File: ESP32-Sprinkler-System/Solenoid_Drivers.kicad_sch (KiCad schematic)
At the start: 40 parts, among them J201 Solenoid, J202 Solenoid, J203 Solenoid, J204 Solenoid, Q201 NCE6005AR, Q202 NCE6005AR, Q203 NCE6005AR, Q204 NCE6005AR, U201 MCP1416T-E/OT, U202 MCP1416T-E/OT, U203 MCP1416T-E/OT, U204 MCP1416T-E/OT

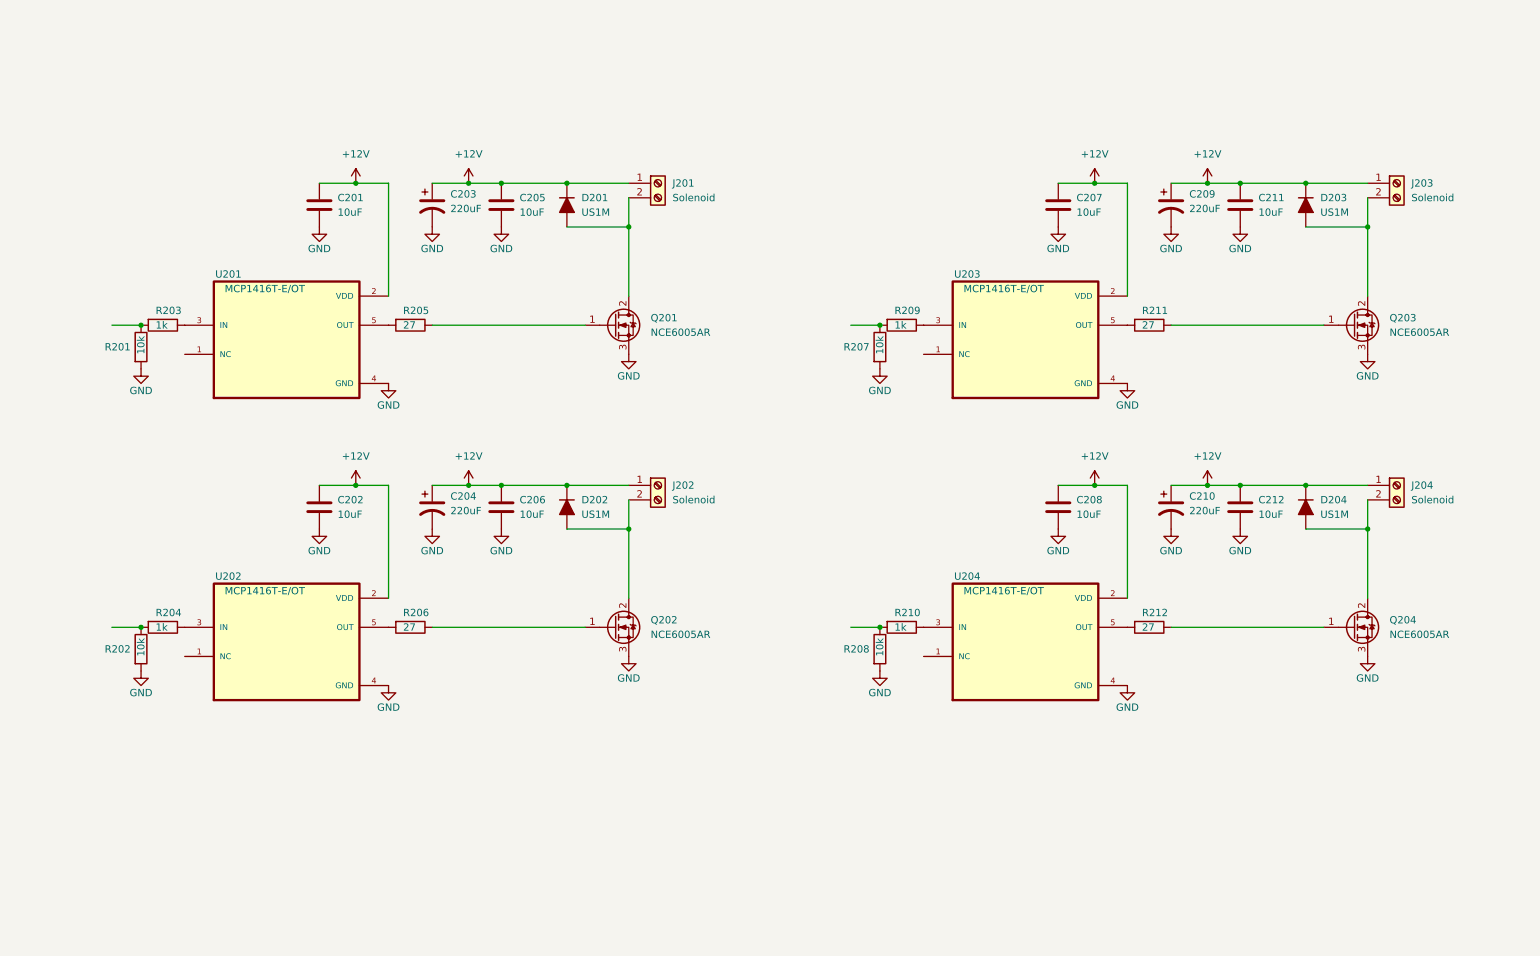
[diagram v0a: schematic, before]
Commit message: Continued working on schematic
finished solenoid drivers, finished buck converter, started ESP32
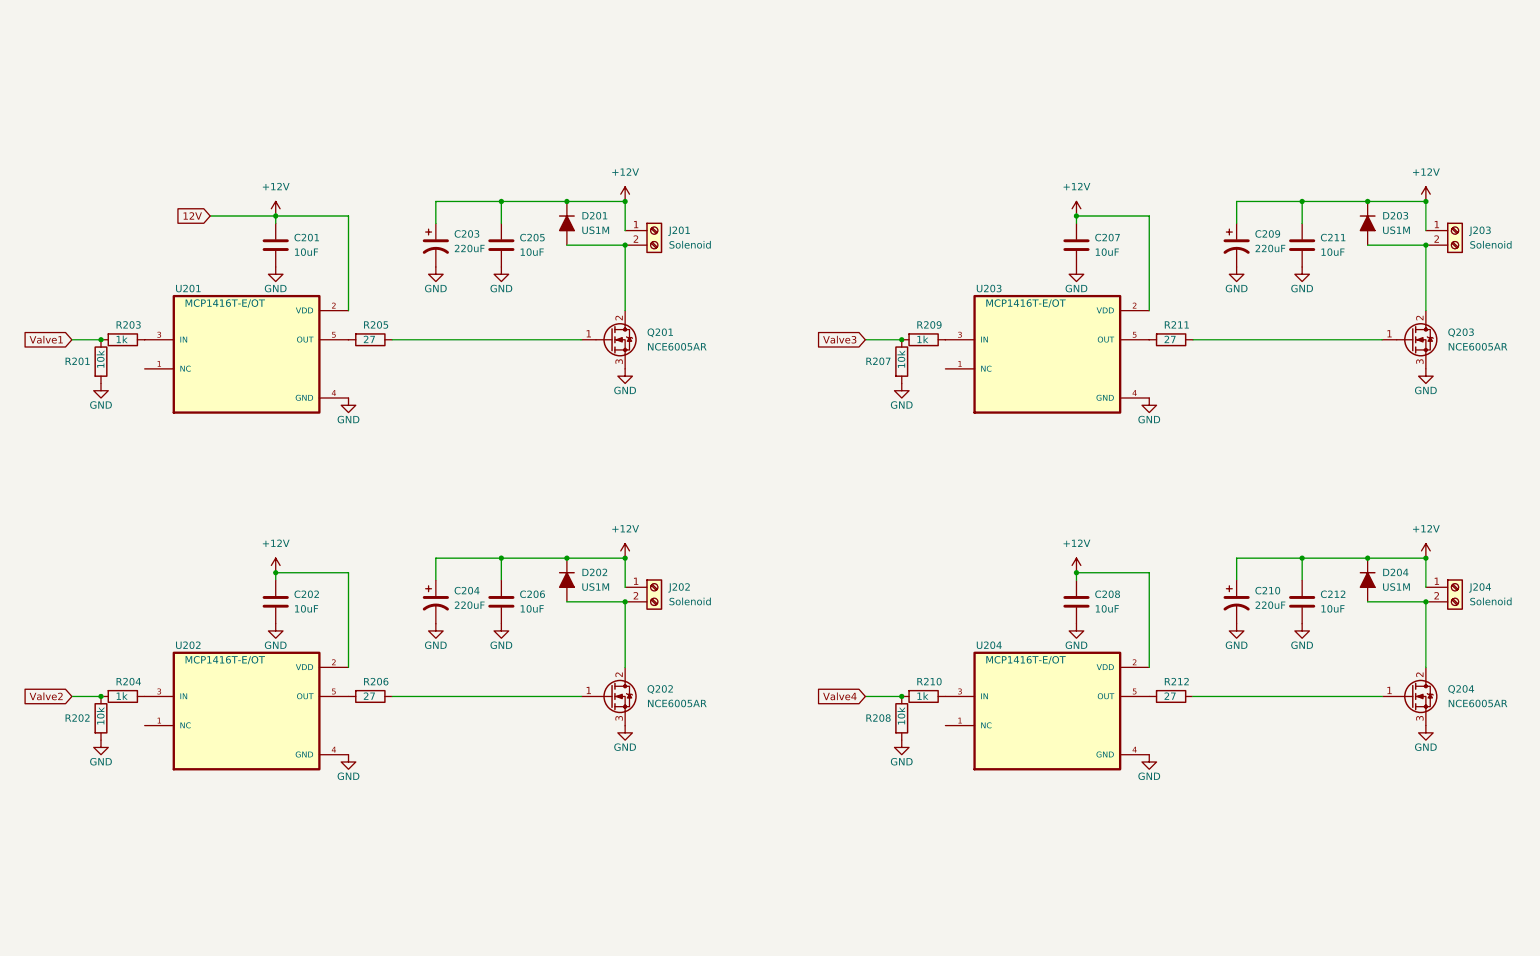
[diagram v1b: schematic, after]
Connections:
- net Valve3: now reaches R207.1, R209.2
- net Valve1: now reaches R201.1, R203.2
- net Valve4: now reaches R208.1, R210.2
- net Valve2: now reaches R202.1, R204.2
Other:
- moved on the sheet: C201, C203, C205, D201, J201, Q201, R201, R203, R205, U201

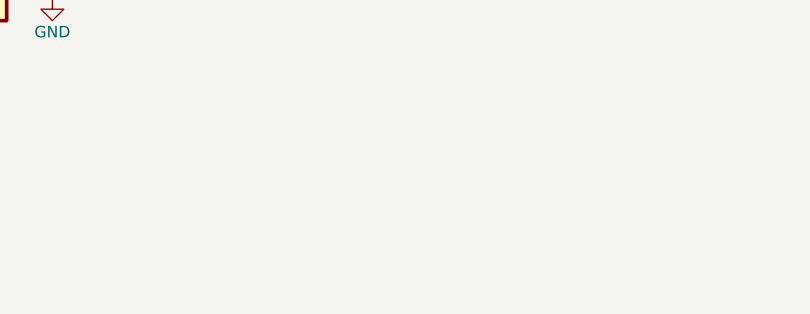
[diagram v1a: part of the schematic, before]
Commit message: Change of plans
We had a change of plans. Rather than having everything made of surface-mount parts, we opted for a simpler through-hole project that could be breadboarded first. This circuit will be revisited and updated when the prototype is complete.
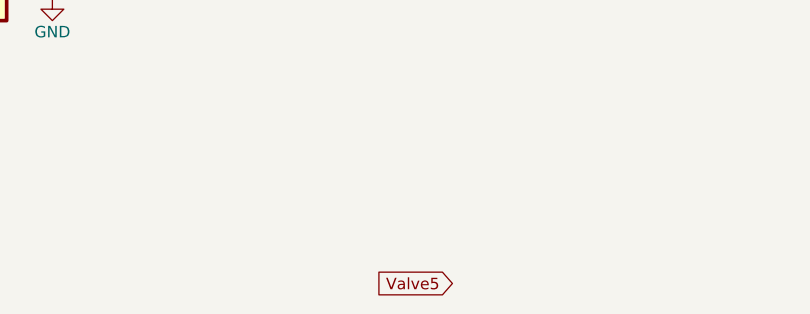
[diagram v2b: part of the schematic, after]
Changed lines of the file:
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@@
+    )
+  )
+  (global_label "Valve5" (shape input) (at 120.65 177.8 180) (fields_autoplaced)
+    (effects (font (size 1.27 1.27)) (justify right))
+    (property "Intersheet References" "${INTERSHEET_REFS}" (id 0) (at 112.0683 177.7206 0)
+      (effects (font (size 1.27 1.27)) (justify right) hide)
     )
   )

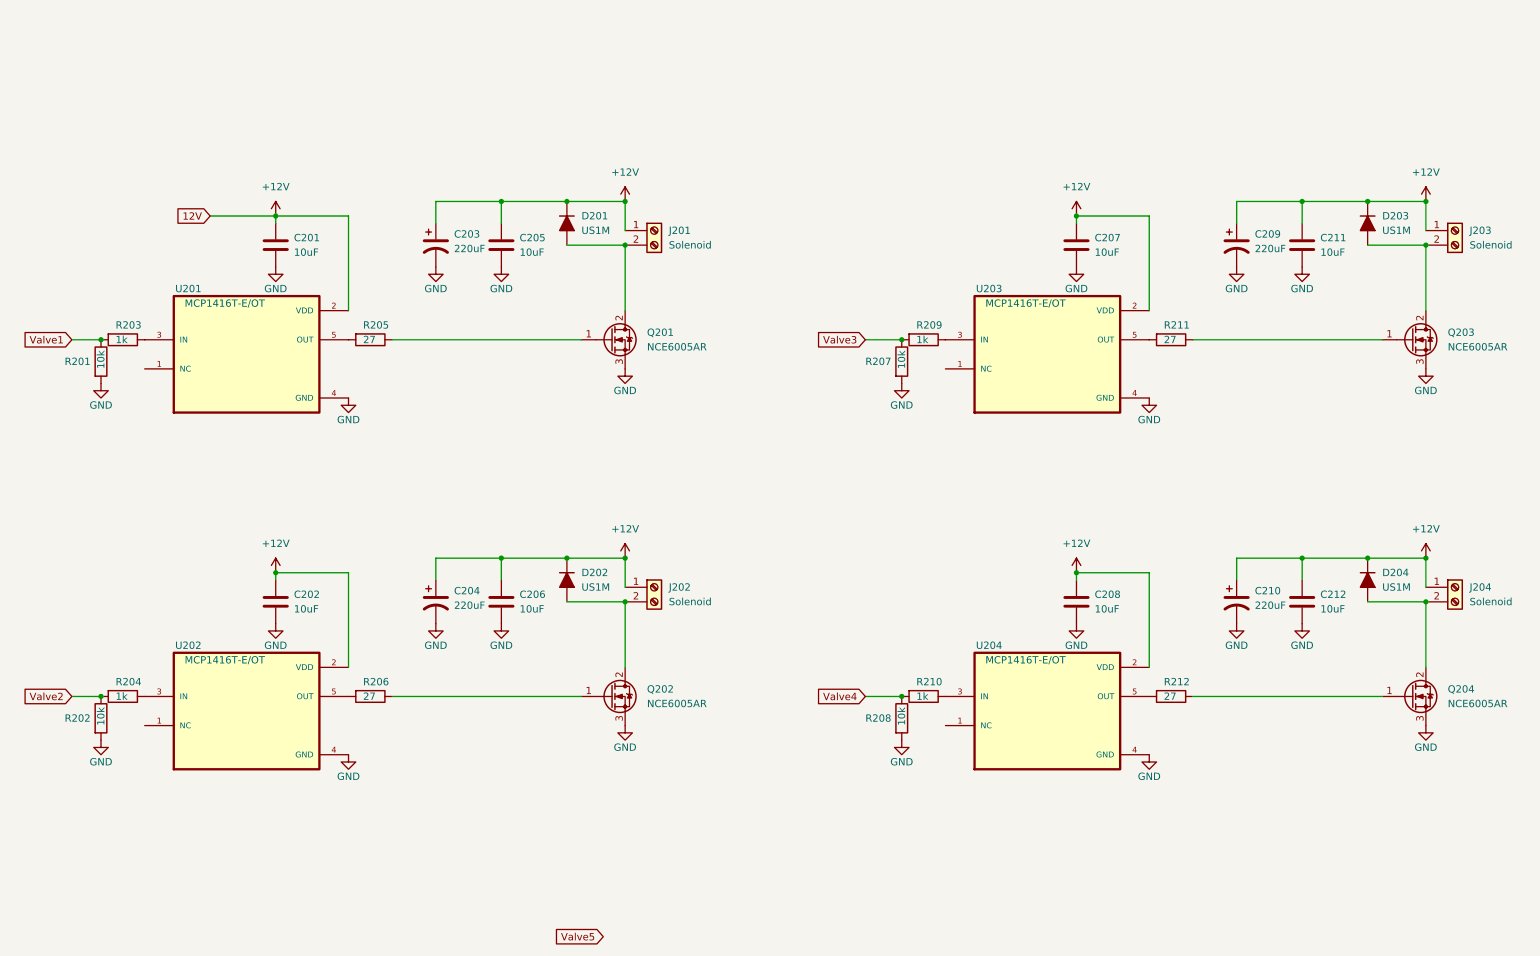
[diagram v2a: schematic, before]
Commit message: Major Update to New Through-Hole Components
Circuit has been modified to match the breadboard prototype Cody built.
Solenoid driver side is done.
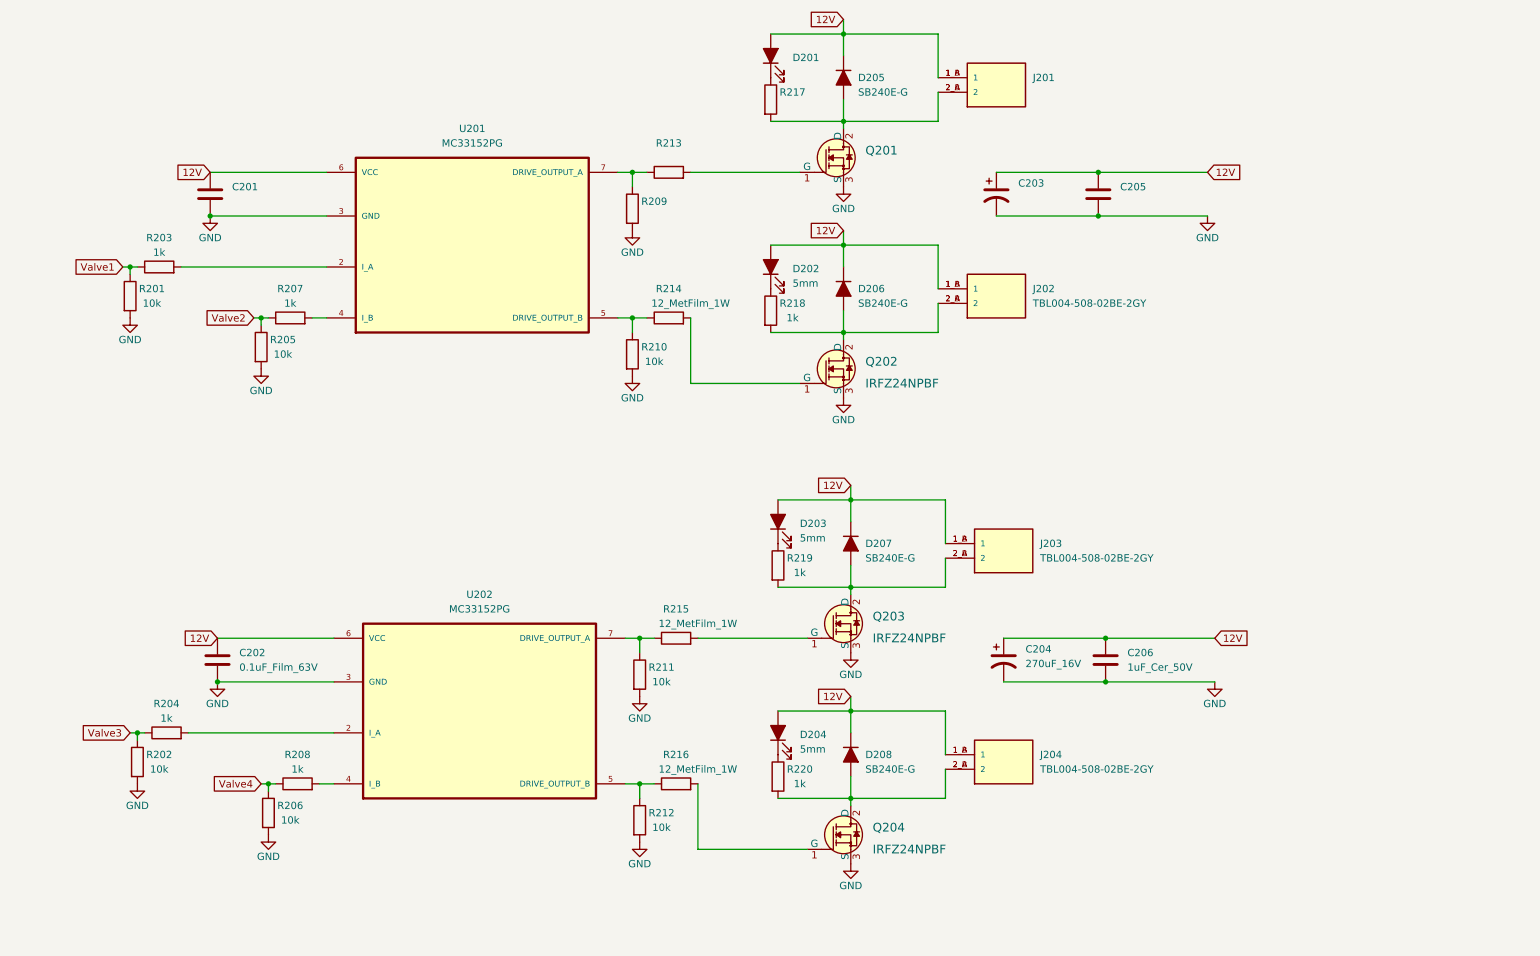
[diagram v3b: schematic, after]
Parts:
- removed C207, C208, C211, C212: 10uF, Capacitor_SMD:C_0603_1608Metric, symbol Device:C
- removed C209, C210: 220uF, Capacitor_SMD:CP_Elec_10x10, symbol Device:C_Polarized_US
- removed D201, D202, D203, D204: US1M, Diode_SMD:D_SMA, symbol Device:D_Filled
- removed J201, J202, J203, J204: Solenoid, Breadstick Footprints:KF202-50-2P, symbol Connector:Screw_Terminal_01x02
- removed Q201, Q202, Q203, Q204: NCE6005AR, Package_TO_SOT_SMD:SOT-223-3_TabPin2, symbol Transistor_FET:BSP89
- removed U201, U202, U203, U204: MCP1416T-E/OT, MCP1416T-E_OT:SOT95P270X145-5N, symbol MCP1416T-E_OT:MCP1416T-E/OT
- added D201: (no value), symbol Device:LED_Filled
- added D202, D203, D204: 5mm, LED_THT:LED_D5.0mm, symbol Device:LED_Filled
- added D205, D206, D207, D208: SB240E-G, Diode_THT:D_DO-15_P12.70mm_Horizontal, symbol Device:D_Filled
- added J201: (no value), symbol TBL004-508-02BE-2GY:TBL004-508-02BE-2GY
- added J202, J203, J204: TBL004-508-02BE-2GY, TBL004-508-02BE-2GY:CUI_TBL004-508-02BE-2GY, symbol TBL004-508-02BE-2GY:TBL004-508-02BE-2GY
- added Q201: (no value), symbol dk_Transistors-FETs-MOSFETs-Single:IRF510PBF
- added Q202, Q203, Q204: IRFZ24NPBF, Package_TO_SOT_THT:TO-220-3_Vertical, symbol dk_Transistors-FETs-MOSFETs-Single:IRF510PBF
- added R213: (no value), symbol Device:R
- added R214, R215, R216: 12_MetFilm_1W, Resistor_THT:R_Axial_DIN0207_L6.3mm_D2.5mm_P10.16mm_Horizontal, symbol Device:R
- added R217: (no value), Resistor_THT:R_Axial_DIN0207_L6.3mm_D2.5mm_P10.16mm_Horizontal, symbol Device:R
- added R218, R219, R220: 1k, Resistor_THT:R_Axial_DIN0207_L6.3mm_D2.5mm_P10.16mm_Horizontal, symbol Device:R
- added U201, U202: MC33152PG, Package_DIP:DIP-8_W7.62mm, symbol MC33152PG:MC33152PG
- C201, C205: value 10uF -> (none); footprint Capacitor_SMD:C_0603_1608Metric -> (none); JLCPCB P/N C96446 -> (none)
- C202: value 10uF -> 0.1uF_Film_63V; footprint Capacitor_SMD:C_0603_1608Metric -> Capacitor_THT:C_Rect_L7.0mm_W2.5mm_P5.00mm; JLCPCB P/N C96446 -> (none)
- C203: value 220uF -> (none); footprint Capacitor_SMD:CP_Elec_10x10 -> (none); JLCPCB P/N C125977 -> (none)
- C204: value 220uF -> 270uF_16V; footprint Capacitor_SMD:CP_Elec_10x10 -> Capacitor_THT:CP_Radial_D6.3mm_P2.50mm; JLCPCB P/N C125977 -> (none)
- C206: value 10uF -> 1uF_Cer_50V; footprint Capacitor_SMD:C_0603_1608Metric -> Capacitor_THT:C_Disc_D7.5mm_W4.4mm_P5.00mm; JLCPCB P/N C96446 -> (none)
- R201, R202: footprint Breadstick Footprints:Perfect_0402_Resistor -> Resistor_THT:R_Axial_DIN0207_L6.3mm_D2.5mm_P10.16mm_Horizontal; JLCPCB P/N C25744 -> (none)
- R203, R204: footprint Breadstick Footprints:Perfect_0402_Resistor -> Resistor_THT:R_Axial_DIN0207_L6.3mm_D2.5mm_P10.16mm_Horizontal; JLCPCB P/N C11702 -> (none)
- R205, R206, R211, R212: value 27 -> 10k; footprint Breadstick Footprints:Perfect_0402_Resistor -> Resistor_THT:R_Axial_DIN0207_L6.3mm_D2.5mm_P10.16mm_Horizontal; JLCPCB P/N C25100 -> (none)
- R207, R208: value 10k -> 1k; footprint Breadstick Footprints:Perfect_0402_Resistor -> Resistor_THT:R_Axial_DIN0207_L6.3mm_D2.5mm_P10.16mm_Horizontal; JLCPCB P/N C25744 -> (none)
- R209: value 1k -> (none); footprint Breadstick Footprints:Perfect_0402_Resistor -> Resistor_THT:R_Axial_DIN0207_L6.3mm_D2.5mm_P10.16mm_Horizontal; JLCPCB P/N C11702 -> (none)
- R210: value 1k -> 10k; footprint Breadstick Footprints:Perfect_0402_Resistor -> Resistor_THT:R_Axial_DIN0207_L6.3mm_D2.5mm_P10.16mm_Horizontal; JLCPCB P/N C11702 -> (none)
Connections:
- net GND: now also R205.2, R206.2, R209.2, R210.2, R211.2, R212.2, Q201.3 (S), Q202.3 (S), Q203.3 (S), Q204.3 (S), U201.3 (GND), U202.3 (GND); no longer R207.2, R208.2
- net Valve1: now also R203.1; no longer R203.2
- net Valve2: now also R205.1, R207.1; no longer R202.1, R204.2
- net Valve3: now also R202.1, R204.1; no longer R207.1, R209.2
- net Valve4: now also R206.1; no longer R210.2
- net at R212.1: now also R216.1, U202.5 (DRIVE_OUTPUT_B)
- net at R209.1: now also R213.1, U201.7 (DRIVE_OUTPUT_A)
- net at R211.1: now also R215.1, U202.7 (DRIVE_OUTPUT_A)
- net at R210.1: now also R214.1, U201.5 (DRIVE_OUTPUT_B)
- net +12V renamed 12V
- net 12V: now also D201.2 (A), D202.2 (A), D203.2 (A), D204.2 (A), D205.1 (K), D206.1 (K), D207.1 (K), D208.1 (K), J201.1_A (1), J201.1_B (1), J202.1_A (1), J202.1_B (1), J203.1_A (1), J203.1_B (1), J204.1_A (1), J204.1_B (1), U201.6 (VCC), U202.6 (VCC)
- new net: D206.2 (A), J202.2_A (2), J202.2_B (2), Q202.2 (D), R218.2
- new net: D202.1 (K), R218.1
- new net: Q204.1 (G), R216.2
- new net: D204.1 (K), R220.1
- new net: D208.2 (A), J204.2_A (2), J204.2_B (2), Q204.2 (D), R220.2
- new net: D207.2 (A), J203.2_A (2), J203.2_B (2), Q203.2 (D), R219.2
- new net: R203.2, U201.2 (I_A)
- new net: Q203.1 (G), R215.2
- new net: R208.2, U202.4 (I_B)
- new net: Q201.1 (G), R213.2
- new net: D205.2 (A), J201.2_A (2), J201.2_B (2), Q201.2 (D), R217.2
- new net: R207.2, U201.4 (I_B)
- new net: D203.1 (K), R219.1
- new net: U201.1 (N.C_2), U201.8 (N.C)
- new net: Q202.1 (G), R214.2
- new net: U202.1 (N.C_2), U202.8 (N.C)
- new net: R204.2, U202.2 (I_A)
- new net: D201.1 (K), R217.1
